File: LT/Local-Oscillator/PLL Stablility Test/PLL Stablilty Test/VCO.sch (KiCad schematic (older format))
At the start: 28 parts

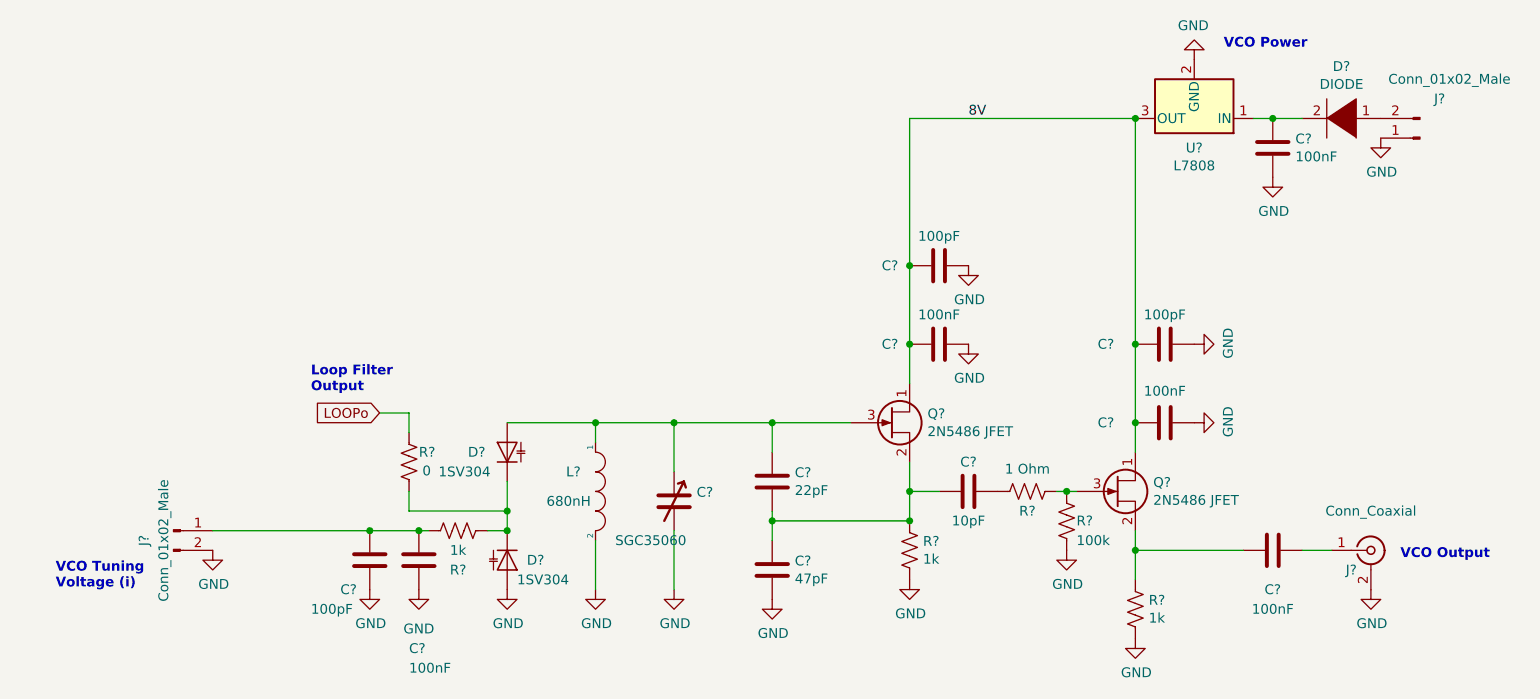
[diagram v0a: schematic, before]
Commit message: completed PLL stability test layour for individual boards
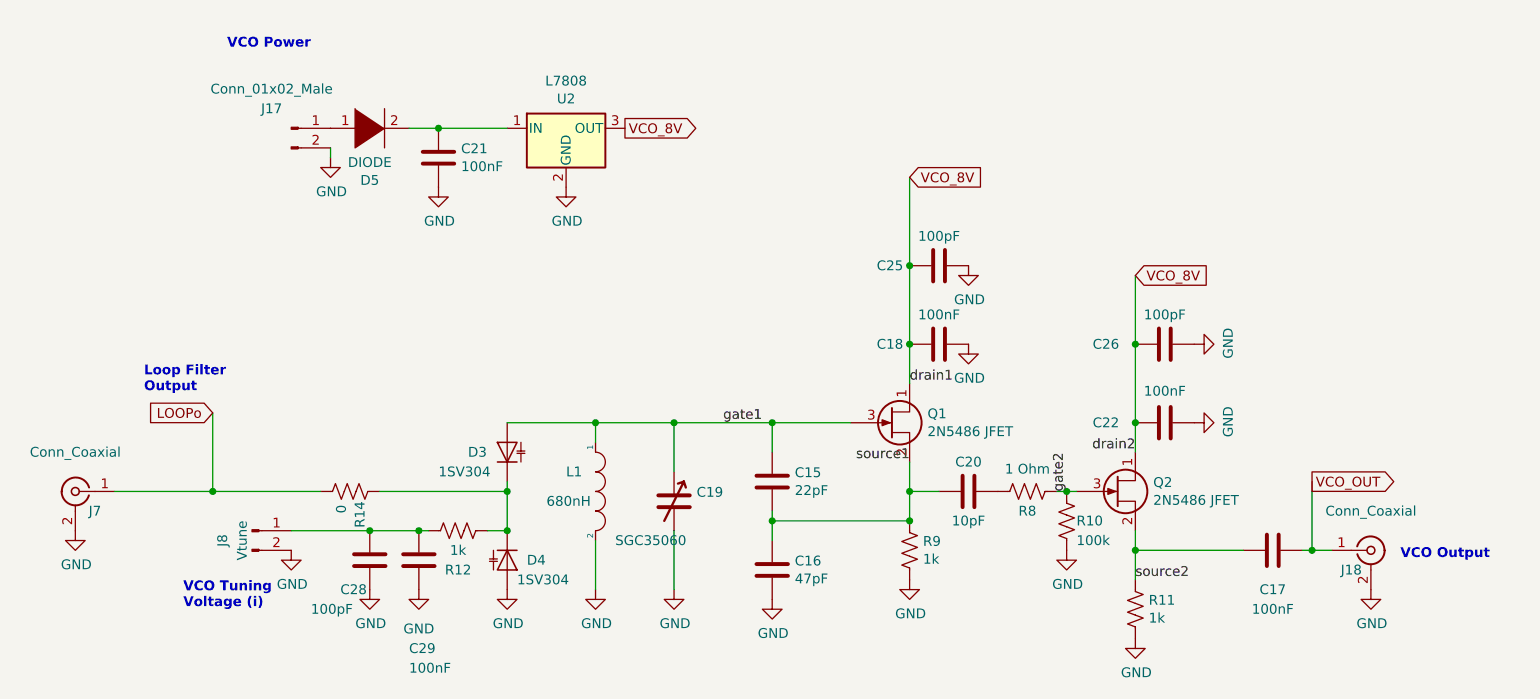
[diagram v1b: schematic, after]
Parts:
- added J7: Conn_Coaxial, Connector_Coaxial:SMA_Molex_73251-1153_EdgeMount_Horizontal, symbol Connector:Conn_Coaxial
- J8: renamed from J?; value Conn_01x02_Male -> Vtune
- gave numbers to parts that had none: 27
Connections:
- net GND: now also J17.2 (Pin_2), J7.2 (Ext); no longer J17.1 (Pin_1)
- net LOOPo: now also R14.2, J7.1 (In); no longer R14.1
- net source2: now reaches C17.1, Q2.2 (S), R11.1
- net gate2: now reaches Q2.3 (G), R10.1, R8.1
- net source1: now reaches C15.1, C16.2, C20.1, Q1.2 (S), R9.1
- net at D3.1 (K), D4.1 (K), R12.1: now also R14.1; no longer R14.2
- net at D5.1 (K): now also J17.1 (Pin_1); no longer J17.2 (Pin_2)
- net gate1: now reaches C15.2, C19.1, D3.2 (A), L1.1, Q1.3 (G)
- net VCO_OUT: now reaches C17.2, J18.1 (In)
- net 8V renamed VCO_8V
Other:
- moved on the sheet: C21, D5, J17, J8, R14, U2
